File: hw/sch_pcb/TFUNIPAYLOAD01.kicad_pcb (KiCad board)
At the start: 2 copper layers, 70.6 x 50.3 mm, 78 parts, among them J1 SM06B-GHS-TB, J2 SM08B-GHS-TB, J3 HEADER_2x03, J4 SM04B-GHS-TB, J5 HEADER_2x15, J6 SM07B-GHS-TB, M1 HOLE, M2 HOLE, M3 HOLE, M4 HOLE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

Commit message: Routed PCB.
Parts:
- moved SW2 42.5 mm to (116.2, 111.5), turned to 0 degrees
- moved SW1 37.8 mm to (116.2, 107.2), turned to 0 degrees
- moved R3 37.0 mm to (120.2, 112.0), turned to 180 degrees
- moved R2 33.0 mm to (120.3, 107.9)
- moved R26 1.77 mm to (136.9, 87.1)
- moved TP1 0.84 mm to (136.6, 98.5)
- moved C10 0.15 mm to (145.3, 112.4)
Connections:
- net /PC5_D1 renamed /LED1
- net /PC6_D2 renamed /LED2
- net /PC7_D3 renamed /LED3
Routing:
- net +3.3V: track 97.3 -> 183.6 mm, vias 2 -> 6
- net /BTN_USER_B: track 17.3 -> 65.9 mm, vias 0 -> 2
- net +5V: track 44.9 -> 91.7 mm
- net /BTN_USER_A: track 9.05 -> 47.5 mm, vias 0 -> 2
- net /MOSI: track 24.8 -> 60.6 mm, vias 2 -> 3
- net /B0: track 0.00 -> 32.6 mm, vias 0 -> 1
- net /C0: track 0.00 -> 28.6 mm, vias 0 -> 1
- net /LED3: track 0.00 -> 27.9 mm, vias 0 -> 2
- net /A0: track 0.00 -> 26.7 mm
- net GND: track 2.73 -> 24.7 mm, vias 2 -> 19
- net +VSW: track 72.5 -> 84.6 mm
- net /LED2: track 22.3 -> 14.2 mm
- net /SDA: track 102.3 -> 94.2 mm
- net /A1: track 35.0 -> 28.8 mm, vias 3 -> 4
- net /SCL: track 89.7 -> 83.6 mm
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- added copper zone on B.Cu, net Net-(U3-LX1)
- added copper zone on B.Cu, net Net-(U3-LX2)
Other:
- rule pad_to_mask_clearance: 0.08 -> 0.05

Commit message: Improve layout.
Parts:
- added G1: LOGO, TF_LOGA:TF, F.Cu at (133.7, 112.4)
- moved R3 0.51 mm to (120.3, 112.5)
- moved SW2 0.33 mm to (116.2, 111.8)
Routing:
- net /BTN_USER_B: track 65.9 -> 62.0 mm
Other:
- board text added: "ThunderFly.cz"
- board text removed: "ThunderFly.cz 2025"

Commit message: Improve layout and graphics.
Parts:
- added G***: LOGO, LOGO, F.Cu at (137.0, 113.0)
- moved G1 5.62 mm to (133.5, 106.8), turned to 30 degrees
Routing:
- net /RX0: track 20.3 -> 21.6 mm
- net GND: vias 19 -> 49
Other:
- board text added: "K"

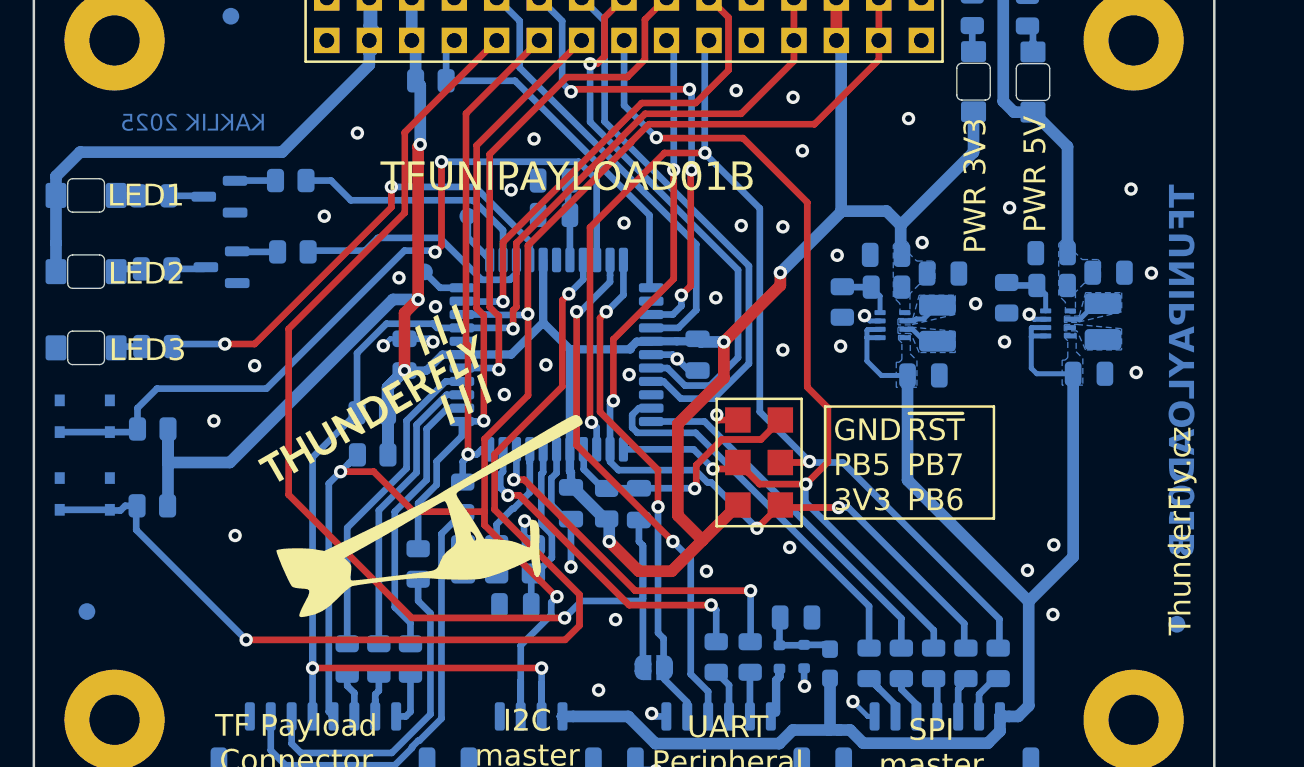
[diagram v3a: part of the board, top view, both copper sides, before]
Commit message: Improve silkscreen.
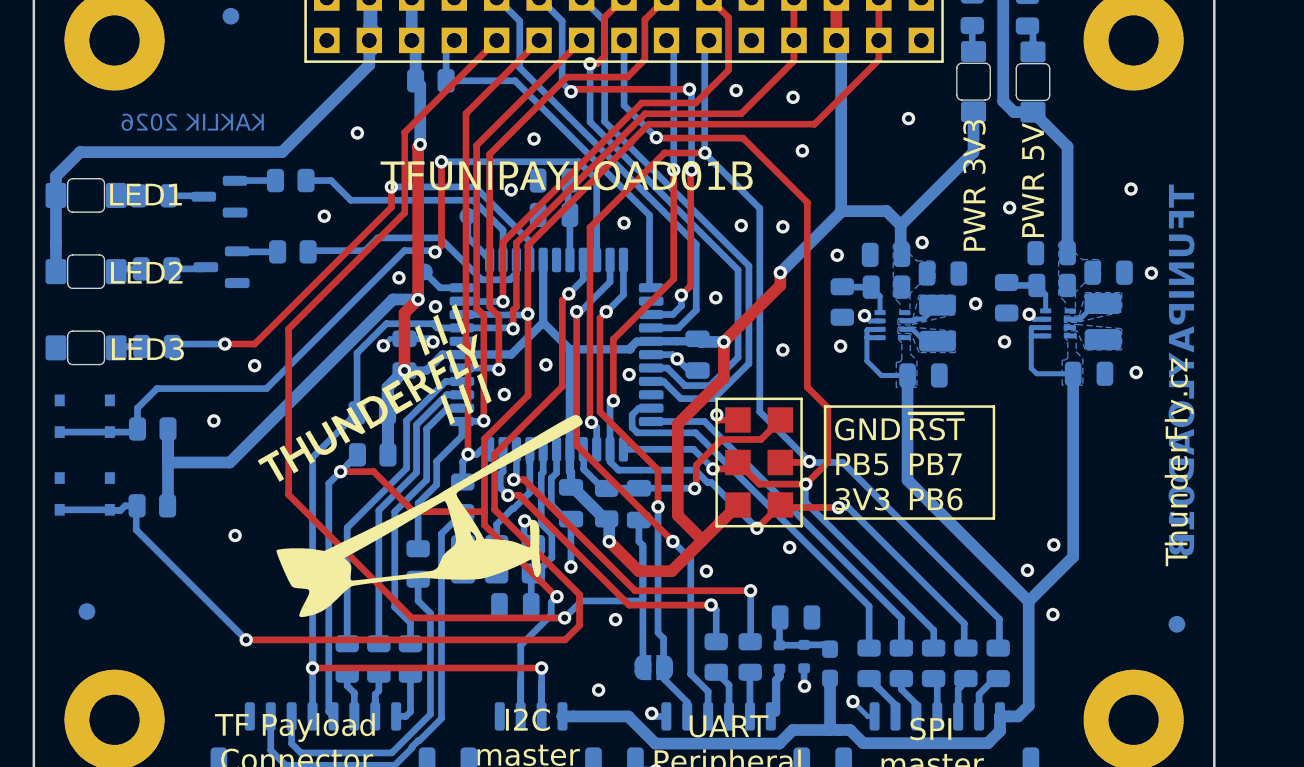
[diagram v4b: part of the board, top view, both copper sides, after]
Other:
- board text added: "KAKLIK 2026"
- board text removed: "KAKLIK 2025"

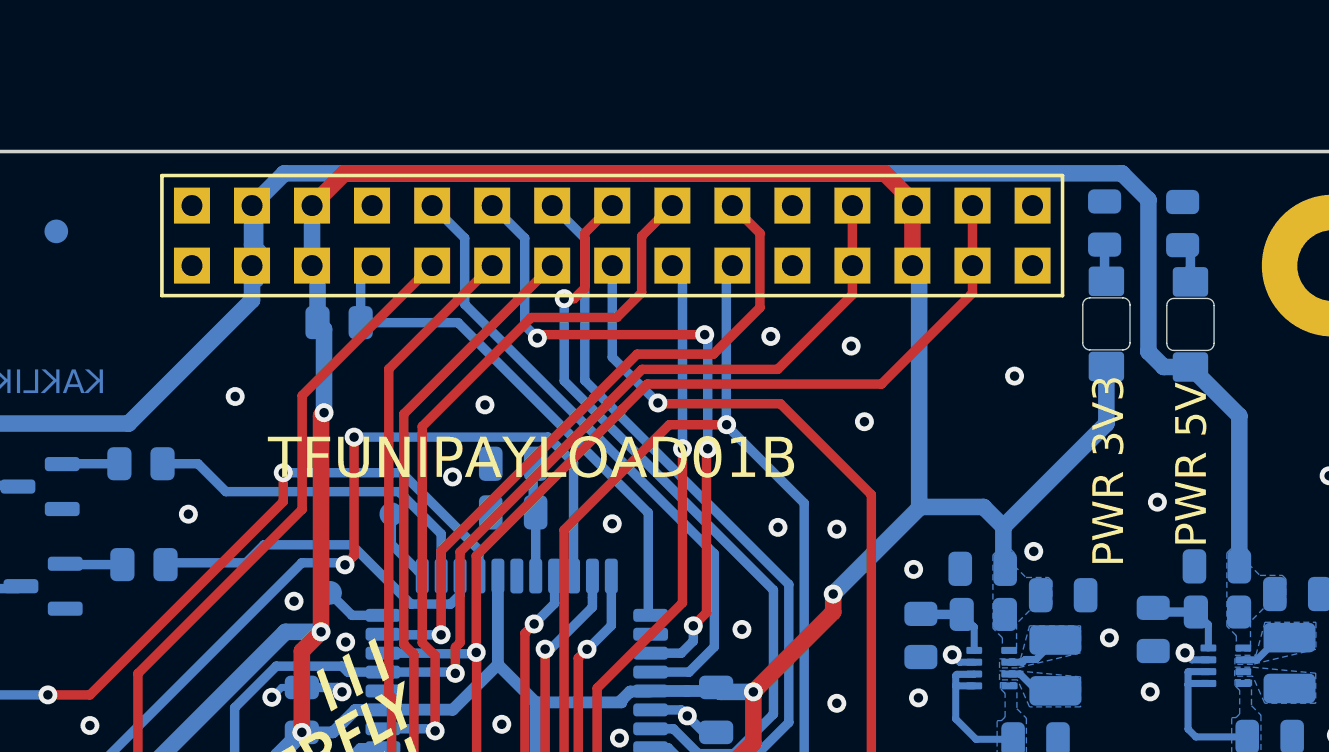
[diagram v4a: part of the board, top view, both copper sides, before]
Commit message: Improve silkscreen.
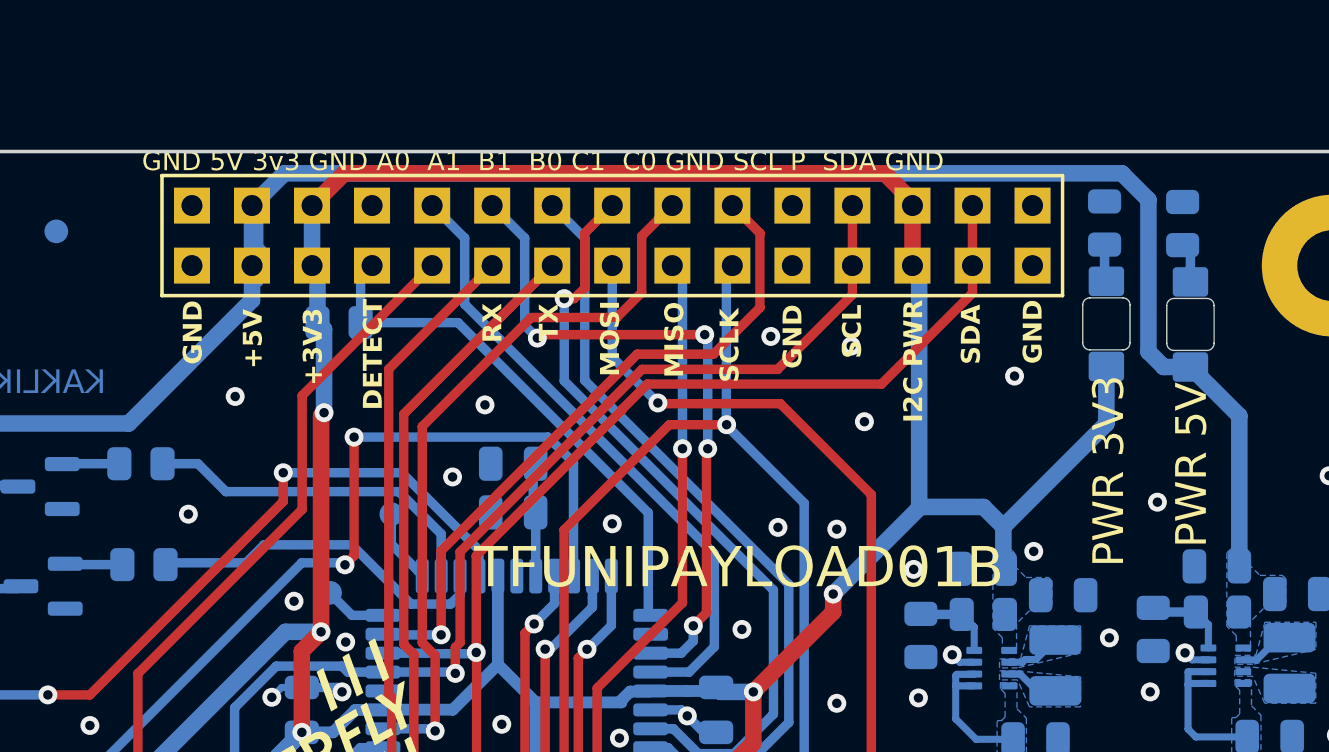
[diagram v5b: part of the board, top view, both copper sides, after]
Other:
- board text added: "+3V3"
- board text added: "+5V"
- board text added: "DETECT"
- board text added: "GND"
- board text added: "GND 5V 3v3 GND A0 A1 B1 B0 C1 C0 GND SCL P SDA GND"
- board text added: "I2C PWR"
- board text added: "MISO"
- board text added: "MOSI"
- board text added: "RX"
- board text added: "SCL"
- board text added: "SCLK"
- board text added: "SDA"
- board text added: "TX"
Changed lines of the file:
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@@
 	)
 	(gr_text "TFUNIPAYLOAD01B"
-		(at 145.1472 92.8334 0)
+		(at 153.8594 97.4562 0)
 		(layer "F.SilkS")
 		(effects
@@
 		)
 	)
+	(gr_text "DETECT"
+		(at 138.848 90.8014 90)
+		(layer "F.SilkS")
+		(effects
+			(font
+				(size 0.8 0.8)
+				(thickness 0.15)
+				(bold yes)
+			)
+			(justify left bottom)
+		)
+	)
 	(gr_text "PWR 5V"
 		(at 173.011 93.1128 90)
@@
 		)
 	)
+	(gr_text "TX"
+		(at 146.2902 87.8804 90)
+		(layer "F.SilkS")
+		(effects
+			(font
+				(size 0.8 0.8)
+				(thickness 0.15)
+				(bold yes)
+			)
+			(justify left bottom)
+		)
+	)
+	(gr_text "MOSI"
+		(at 148.881 89.379 90)
+		(layer "F.SilkS")
+		(effects
+			(font
+				(size 0.8 0.8)
+				(thickness 0.15)
+				(bold yes)
+			)
+			(justify left bottom)
+		)
+	)
+	(gr_text "GND 5V 3v3 GND A0  A1  B1  B0 C1  C0 GND SCL P  SDA GND"
+		(at 128.598 80.7394 0)
+		(layer "F.SilkS")
+		(effects
+			(font
+				(size 0.8 0.8)
+				(thickness 0.1)
+			)
+			(justify left bottom)
+		)
+	)
 	(gr_text "UART\nPeripheral"
 		(at 154.6976 126.7972 0)
@@
 		)
 	)
+	(gr_text "I2C PWR"
+		(at 161.708 91.3348 90)
+		(layer "F.SilkS")
+		(effects
+			(font
+				(size 0.8 0.8)
+				(thickness 0.15)
+				(bold yes)
+			)
+			(justify left bottom)
+		)
+	)
+	(gr_text "RX"
+		(at 143.9026 87.9566 90)
+		(layer "F.SilkS")
+		(effects
+			(font
+				(size 0.8 0.8)
+				(thickness 0.15)
+				(bold yes)
+			)
+			(justify left bottom)
+		)
+	)
+	(gr_text "MISO"
+		(at 151.5988 89.4298 90)
+		(layer "F.SilkS")
+		(effects
+			(font
+				(size 0.8 0.8)
+				(thickness 0.15)
+				(bold yes)
+			)
+			(justify left bottom)
+		)
+	)
+	(gr_text "SCL"
+		(at 159.1172 88.617 90)
+		(layer "F.SilkS")
+		(effects
+			(font
+				(size 0.8 0.8)
+				(thickness 0.15)
+				(bold yes)
+			)
+			(justify left bottom)
+		)
+	)
 	(gr_text "PWR 3V3"
 		(at 169.5058 93.3668 90)
@@
 		)
 	)
+	(gr_text "GND"
+		(at 131.228 88.871 90)
+		(layer "F.SilkS")
+		(effects
+			(font
+				(size 0.8 0.8)
+				(thickness 0.15)
+				(bold yes)
+			)
+			(justify left bottom)
+		)
+	)
 	(gr_text "~{RST}\nPB7\nPB6"
 		(at 165.4234 110.0804 0)
@@
 		)
 	)
+	(gr_text "SDA"
+		(at 164.1464 88.871 90)
+		(layer "F.SilkS")
+		(effects
+			(font
+				(size 0.8 0.8)
+				(thickness 0.15)
+				(bold yes)
+			)
+			(justify left bottom)
+		)
+	)
 	(gr_text "LED1"
 		(at 119.8996 93.951 0)
@@
 		)
 	)
+	(gr_text "GND"
+		(at 166.7626 88.8456 90)
+		(layer "F.SilkS")
+		(effects
+			(font
+				(size 0.8 0.8)
+				(thickness 0.15)
+				(bold yes)
+			)
+			(justify left bottom)
+		)
+	)
+	(gr_text "GND"
+		(at 156.6026 89.0488 90)
+		(layer "F.SilkS")
+		(effects
+			(font
+				(size 0.8 0.8)
+				(thickness 0.15)
+				(bold yes)
+			)
+			(justify left bottom)
+		)
+	)
 	(gr_text "SPI\nmaster"
 		(at 166.8804 128.7702 0)
@@
 		)
 	)
+	(gr_text "+3V3"
+		(at 136.308 89.76 90)
+		(layer "F.SilkS")
+		(effects
+			(font
+				(size 0.8 0.8)
+				(thickness 0.15)
+				(bold yes)
+			)
+			(justify left bottom)
+		)
+	)
 	(gr_text "LED3"
 		(at 120.0012 103.1966 0)
@@
 		)
 	)
+	(gr_text "+5V"
+		(at 133.768 89.0488 90)
+		(layer "F.SilkS")
+		(effects
+			(font
+				(size 0.8 0.8)
+				(thickness 0.15)
+				(bold yes)
+			)
+			(justify left bottom)
+		)
+	)
+	(gr_text "SCLK"
+		(at 153.9356 89.633 90)
+		(layer "F.SilkS")
+		(effects
+			(font
+				(size 0.8 0.8)
+				(thickness 0.15)
+				(bold yes)
+			)
+			(justify left bottom)
+		)
+	)

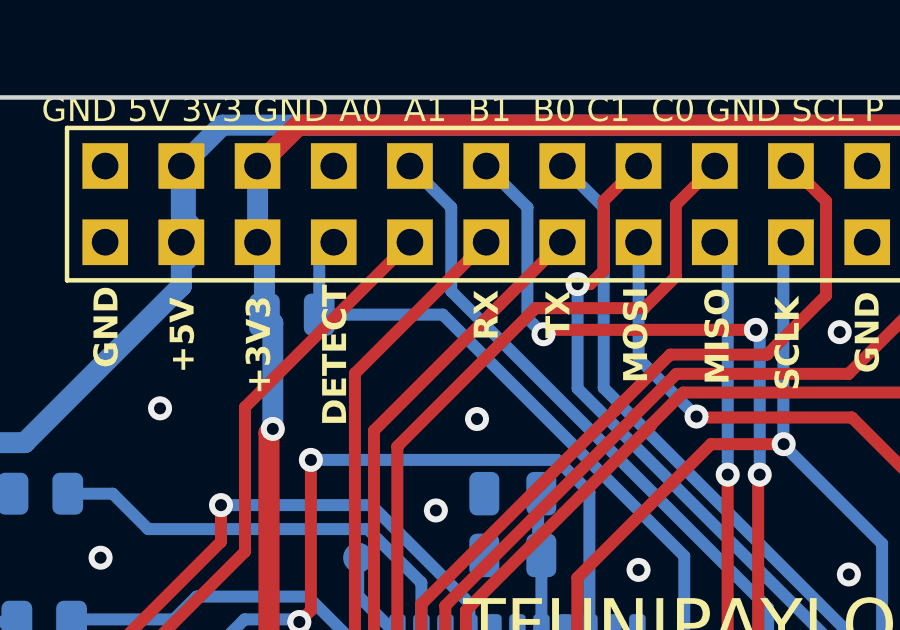
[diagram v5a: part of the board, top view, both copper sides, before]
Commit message: Improve connector description.
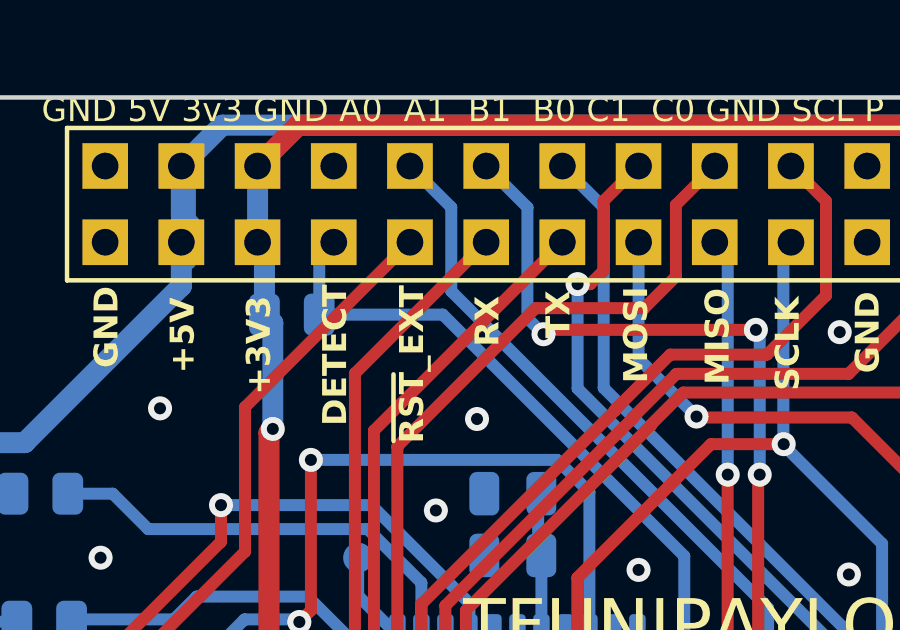
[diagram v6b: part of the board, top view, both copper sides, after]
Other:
- board text added: "~{RST}_EXT"
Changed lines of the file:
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@@
 	)
 	(gr_text "RX"
-		(at 143.9026 87.9566 90)
+		(at 143.928 88.1598 90)
 		(layer "F.SilkS")
 		(effects
+			(font
+				(size 0.8 0.8)
+				(thickness 0.15)
+				(bold yes)
+			)
+			(justify left bottom)
+		)
+	)
+	(gr_text "~{RST}_EXT"
+		(at 141.4134 91.3856 90)
+		(layer "F.SilkS")
+		(effects
